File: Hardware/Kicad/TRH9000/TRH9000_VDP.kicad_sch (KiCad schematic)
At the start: 22 parts, among them U1 V9990, U2 KM428C256, U3 KM428C256, X1 14.318Mhz, Y1 21.47727Mhz

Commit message: Footprint for the V9990
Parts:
- C2: footprint (none) -> Capacitor_SMD:C_0805_2012Metric
- U1: footprint Ddraig:QFP-128_28x28_Pitch0.8mm -> trh9000:QFP-128_28x28_Pitch0.8mm
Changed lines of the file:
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@@
       (effects (font (size 1.27 1.27)) (justify left))
     )
-    (property "Footprint" "Ddraig:QFP-128_28x28_Pitch0.8mm" (id 2) (at 129.54 135.89 0)
+    (property "Footprint" "trh9000:QFP-128_28x28_Pitch0.8mm" (id 2) (at 129.54 135.89 0)
       (effects (font (size 1.27 1.27)) hide)
     )
@@
       (effects (font (size 1.27 1.27)) (justify left))
     )
-    (property "Footprint" "" (id 2) (at 49.2252 250.19 0)
+    (property "Footprint" "Capacitor_SMD:C_0805_2012Metric" (id 2) (at 49.2252 250.19 0)
       (effects (font (size 1.27 1.27)) hide)
     )

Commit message: Trimpots for the RGB coming from V9990
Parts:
- Y1: footprint Crystal:Crystal_HC50_Vertical -> Crystal:Crystal_HC49-U_Vertical
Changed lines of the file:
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@@
     (property "Reference" "Y1" (id 0) (at 54.61 145.5928 0))
     (property "Value" "21.47727Mhz" (id 1) (at 54.61 147.9042 0))
-    (property "Footprint" "Crystal:Crystal_HC50_Vertical" (id 2) (at 54.61 152.4 0)
+    (property "Footprint" "Crystal:Crystal_HC49-U_Vertical" (id 2) (at 54.61 152.4 0)
       (effects (font (size 1.27 1.27)) hide)
     )

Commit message: REV0 - Footprint Review
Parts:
- R1, R2, R3, R4, R5, R6: footprint LED_SMD:LED_0805_2012Metric -> Resistor_SMD:R_0805_2012Metric
- U2, U3: footprint (none) -> trh9000:TSOP-II-40_10.16x18.41mm_P0.8mm
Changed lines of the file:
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@@
       (effects (font (size 1.27 1.27)) (justify left))
     )
-    (property "Footprint" "" (id 2) (at 292.1 207.01 0)
+    (property "Footprint" "trh9000:TSOP-II-40_10.16x18.41mm_P0.8mm" (id 2) (at 292.1 207.01 0)
       (effects (font (size 1.27 1.27)) hide)
     )
@@
       (effects (font (size 1.27 1.27)) (justify left))
     )
-    (property "Footprint" "LED_SMD:LED_0805_2012Metric" (id 2) (at 51.562 83.82 90)
+    (property "Footprint" "Resistor_SMD:R_0805_2012Metric" (id 2) (at 51.562 83.82 90)
       (effects (font (size 1.27 1.27)) hide)
     )
@@
       (effects (font (size 1.27 1.27)) (justify left))
     )
-    (property "Footprint" "" (id 2) (at 292.1 100.33 0)
+    (property "Footprint" "trh9000:TSOP-II-40_10.16x18.41mm_P0.8mm" (id 2) (at 292.1 100.33 0)
       (effects (font (size 1.27 1.27)) hide)
     )
@@
       (effects (font (size 1.27 1.27)) (justify left))
     )
-    (property "Footprint" "LED_SMD:LED_0805_2012Metric" (id 2) (at 82.042 146.05 90)
+    (property "Footprint" "Resistor_SMD:R_0805_2012Metric" (id 2) (at 82.042 146.05 90)
       (effects (font (size 1.27 1.27)) hide)
     )
@@
       (effects (font (size 1.27 1.27)) (justify left))
     )
-    (property "Footprint" "LED_SMD:LED_0805_2012Metric" (id 2) (at 59.182 83.82 90)
+    (property "Footprint" "Resistor_SMD:R_0805_2012Metric" (id 2) (at 59.182 83.82 90)
       (effects (font (size 1.27 1.27)) hide)
     )
@@
       (effects (font (size 1.27 1.27)) (justify left))
     )
-    (property "Footprint" "LED_SMD:LED_0805_2012Metric" (id 2) (at 43.942 83.82 90)
+    (property "Footprint" "Resistor_SMD:R_0805_2012Metric" (id 2) (at 43.942 83.82 90)
       (effects (font (size 1.27 1.27)) hide)
     )
@@
     (property "Reference" "R3" (id 0) (at 54.61 135.7122 90))
     (property "Value" "10M" (id 1) (at 54.61 138.0236 90))
-    (property "Footprint" "LED_SMD:LED_0805_2012Metric" (id 2) (at 54.61 139.192 90)
+    (property "Footprint" "Resistor_SMD:R_0805_2012Metric" (id 2) (at 54.61 139.192 90)
       (effects (font (size 1.27 1.27)) hide)
     )
@@
       (effects (font (size 1.27 1.27)) (justify left))
     )
-    (property "Footprint" "LED_SMD:LED_0805_2012Metric" (id 2) (at 74.422 146.05 90)
-      (effects (font (size 1.27 1.27)) hide)
-    )
+    (property "Footprint" "Resistor_SMD:R_0805_2012Metric" (id 2) (at 74.422 146.05 90)
+      (effects (font (size 1.27 1.27)) hide)
+    )

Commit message: Routing 1. First 3d view of the current PCB.
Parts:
- U2, U3: footprint trh9000:TSOP-II-40_10.16x18.41mm_P0.8mm -> trh9000:SOJ-40_400mil
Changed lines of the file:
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@@
       (effects (font (size 1.27 1.27)) (justify left))
     )
-    (property "Footprint" "trh9000:TSOP-II-40_10.16x18.41mm_P0.8mm" (id 2) (at 292.1 207.01 0)
+    (property "Footprint" "trh9000:SOJ-40_400mil" (id 2) (at 292.1 207.01 0)
       (effects (font (size 1.27 1.27)) hide)
     )
@@
       (effects (font (size 1.27 1.27)) (justify left))
     )
-    (property "Footprint" "trh9000:TSOP-II-40_10.16x18.41mm_P0.8mm" (id 2) (at 292.1 100.33 0)
+    (property "Footprint" "trh9000:SOJ-40_400mil" (id 2) (at 292.1 100.33 0)
       (effects (font (size 1.27 1.27)) hide)
     )

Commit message: Many changes, among them, replacing the Composite out with SCART-rgb.
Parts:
- removed C2, C5, C6, C7, C8, C9: 100nF, Capacitor_SMD:C_0805_2012Metric, symbol Device:C
- removed C3: 47uF, Capacitor_THT:CP_Radial_D5.0mm_P2.50mm, symbol Device:C_Polarized
- removed L1, L2: 4.7uH, Inductor_SMD:L_1206_3216Metric, symbol pspice:INDUCTOR
- added unit 3 of U1
- added unit 2 of U1
- U1: footprint trh9000:QFP-128_28x28_Pitch0.8mm -> trh9000:LQFP-128_28x28mm_P0.8mm; MPN (none) -> V9990; Manufacturer (none) -> Yamaha
- U2, U3: Manufacturer (none) -> Samsung Electronics Inc.; Status (none) -> OBSOLETE
- X1: value 14.318Mhz -> Crystek_CE3291; footprint Oscillator:Oscillator_DIP-8 -> Oscillator:Oscillator_SMD_Abracon_ASV-4Pin_7.0x5.1mm; symbol Oscillator:CXO_DIP8 -> TRH9000:Crystek_CE3291; Frequency (none) -> 14.31818MHz; MPN (none) -> CE3291-14.318180; Manufacturer (none) -> Crystek Corporation
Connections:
- net +5V: now also R6.2, X1.4 (Vcc); no longer R6.1, U1.123 (VCC), U1.27 (VCC), U1.53 (VCC), U1.81 (VCC), U1.97 (VCC), U2.1 (VCC), U2.20 (VCC), U3.1 (VCC), U3.20 (VCC), X1.8 (Vcc)
- net B: now also U1.95 (B/D1/CB1); no longer U1.95 (B/D31/CB1)
- net G: now also U1.94 (G/D2/CB2); no longer U1.94 (G/D2/CB2)
- net GND: now also X1.2 (GND); no longer U1.1 (GND), U1.100 (GND), U1.107 (GND), U1.118 (GND), U1.17 (GND), U1.32 (GND), U1.44 (GND), U1.64 (GND), U1.75 (GND), U1.86 (GND), U2.12 (VSS), U2.21 (VSS), U2.30 (VSS), U2.40 (VSS), U3.12 (VSS), U3.21 (VSS), U3.30 (VSS), U3.40 (VSS), X1.4 (GND)
- net R: now also U1.93 (R/D3/CB3); no longer U1.93 (R/D3/CB3)
- net V0A0: now also U1.26 (V0_A0/KA0); no longer U1.26 (V0A0/KA0)
- net V0A1: now also U1.25 (V0_A1/KA1); no longer U1.25 (V0A1/KA1)
- net V0A2: now also U1.24 (V0_A2/KA2); no longer U1.24 (V0A2/KA2)
- net V0A3: now also U1.23 (V0_A3/KA3); no longer U1.23 (V0A3/KA3)
- net V0A4: now also U1.22 (V0_A4/KA4); no longer U1.22 (V0A4/KA4)
- net V0A5: now also U1.21 (V0_A5/KA5); no longer U1.21 (V0A5/KA5)
- net V0A6: now also U1.20 (V0_A6/KA6); no longer U1.20 (V0A6/KA6)
- net V0A7: now also U1.19 (V0_A7/KA7); no longer U1.19 (V0A7/KA7)
- net V0A8: now also U1.18 (V0_A8/KA8); no longer U1.18 (V0A8/KA8)
- net V0D0: now also U1.36 (V0_D0/KD0); no longer U1.36 (V0D0/DK0)
- net V0D1: now also U1.35 (V0_D1/KD1); no longer U1.35 (V0D1/DK1)
- net V0D2: now also U1.34 (V0_D2/KD2); no longer U1.34 (V0D2/DK2)
- net V0D3: now also U1.33 (V0_D3/KD3); no longer U1.33 (V0D3/DK3)
- net V0D4: now also U1.31 (V0_D4/KD4); no longer U1.31 (V0D4/DK4)
- net V0D5: now also U1.30 (V0_D5/KD5); no longer U1.30 (V0D5/DK5)
- net V0D6: now also U1.29 (V0_D6/KD6); no longer U1.29 (V0D6/DK6)
- net V0D7: now also U1.28 (V0_D7/KD7); no longer U1.28 (V0D7/DK7)
- net V0S0: now also U1.52 (V0_S0); no longer U1.52 (V0S0)
- net V0S1: now also U1.51 (V0_S1); no longer U1.51 (V0S1)
- net V0S2: now also U1.50 (V0_S2); no longer U1.50 (V0S2)
- net V0S3: now also U1.49 (V0_S3); no longer U1.49 (V0S3)
- net V0S4: now also U1.48 (V0_S4); no longer U1.48 (V0S4)
- net V0S5: now also U1.47 (V0_S5); no longer U1.47 (V0S5)
- net V0S6: now also U1.46 (V0_S6); no longer U1.46 (V0S6)
- net V0S7: now also U1.45 (V0_S7); no longer U1.45 (V0S7)
- net V1A0: now also U1.80 (V1_A0); no longer U1.80 (V1A0)
- net V1A1: now also U1.79 (V1_A1); no longer U1.79 (V1A1)
- net V1A2: now also U1.78 (V1_A2); no longer U1.78 (V1A2)
- net V1A3: now also U1.77 (V1_A3); no longer U1.77 (V1A3)
- net V1A4: now also U1.76 (V1_A4); no longer U1.76 (V1A4)
- net V1A5: now also U1.74 (V1_A5); no longer U1.74 (V1A5)
- net V1A6: now also U1.73 (V1_A6); no longer U1.73 (V1A6)
- net V1A7: now also U1.72 (V1_A7); no longer U1.72 (V1A7)
- net V1A8: now also U1.71 (V1_A8); no longer U1.71 (V1A8)
- net V1D0: now also U1.82 (V1_D0); no longer U1.82 (V1D0)
- net V1D1: now also U1.83 (V1_D1); no longer U1.83 (V1D1)
- net V1D2: now also U1.84 (V1_D2); no longer U1.84 (V1D2)
- net V1D3: now also U1.85 (V1_D3); no longer U1.85 (V1D3)
- net V1D4: now also U1.87 (V1_D4); no longer U1.87 (V1D4)
- net V1D5: now also U1.88 (V1_D5); no longer U1.88 (V1D5)
- net V1D6: now also U1.89 (V1_D6); no longer U1.89 (V1D6)
- net V1D7: now also U1.90 (V1_D7); no longer U1.90 (V1D7)
- net V1S0: now also U1.61 (V1_S0); no longer U1.61 (V1S0)
- net V1S1: now also U1.60 (V1_S1); no longer U1.60 (V1S1)
- net V1S2: now also U1.59 (V1_S2); no longer U1.59 (V1S2)
- net V1S3: now also U1.58 (V1_S3); no longer U1.58 (V1S3)
- net V1S4: now also U1.57 (V1_S4); no longer U1.57 (V1S4)
- net V1S5: now also U1.56 (V1_S5); no longer U1.56 (V1S5)
- net V1S6: now also U1.55 (V1_S6); no longer U1.55 (V1S6)
- net V1S7: now also U1.54 (V1_S7); no longer U1.54 (V1S7)
- net ~{CSYNC}: now also U1.102 (~{CSYNC/FLM}); no longer U1.102 (~{CSYNC}/FLM)
- net ~{VDPR}: now also U1.2 (~{CSW}); no longer U1.3 (~{CSR})
- net ~{VDPW}: now also U1.3 (~{CSR}); no longer U1.2 (~{CSW})
- net X2: now reaches C4.1, R3.1, Y1.2
- net X2: now also U1.99 (XTAL2); no longer U1.99 (XTAL2)
- net ~{V0_WE}: now reaches U3.13 (R~{WB}/~{WE})
- net ~{V0_WE}: now also U1.40 (~{V0_WE}); no longer U1.40 (~{V0WE})
- net ~{V0_RAS}: now reaches U3.14 (~{RAS})
- net ~{V0_RAS}: now also U1.38 (~{V0_RAS}); no longer U1.38 (~{V0RAS})
- net ~{V0_SC}: now reaches U3.2 (SC)
- net ~{V0_SC}: now also U1.42 (~{V0_SC}); no longer U1.42 (V0SC)
- net ~{V0_CAS}: now reaches U3.27 (~{CAS})
- net ~{V0_CAS}: now also U1.39 (~{V0_CAS}); no longer U1.39 (~{V0CAS})
- net ~{VO_SOE}: now reaches U3.35 (~{SE})
- net ~{VO_SOE}: now also U1.43 (~{V0_SOE}); no longer U1.43 (~{V0SOE})
- net ~{V0_TR}: now reaches U3.7 (~{DT}/~{OE})
- net ~{V0_TR}: now also U1.41 (~{V0_TR/OE}); no longer U1.41 (~{V0TR}/~{OE})
- net X1: now reaches C1.1, R3.2, Y1.1
- net X1: now also U1.98 (XTAL1); no longer U1.98 (XTAL1)
- net ~{V1_WE}: now reaches U2.13 (R~{WB}/~{WE})
- net ~{V1_WE}: now also U1.65 (~{V1_WE}); no longer U1.65 (~{V1WE})
- net ~{V1_RAS}: now reaches U2.14 (~{RAS})
- net ~{V1_RAS}: now also U1.62 (~{V1_RAS}); no longer U1.62 (~{V1RAS})
- net ~{V1_SC}: now reaches U2.2 (SC)
- net ~{V1_SC}: now also U1.67 (V1_SC); no longer U1.67 (V1SC)
- net ~{V1_CAS}: now reaches U2.27 (~{CAS})
- net ~{V1_CAS}: now also U1.63 (~{V1_CAS}); no longer U1.63 (~{V1CAS})
- net ~{V1_SOE}: now reaches U2.35 (~{SE})
- net ~{V1_SOE}: now also U1.68 (~{V1_SOE}); no longer U1.68 (~{V1SOE})
- net ~{V1_TR}: now reaches U2.7 (~{DT}/~{OE})
- net ~{V1_TR}: now also U1.66 (~{V1_TR/OE}); no longer U1.66 (~{V1TR}/~{OE})
- net HRESET: now reaches R5.2
- net HRESET: now also U1.105 (~{HRESET}/CB4); no longer U1.106 (~{VRESET}/CB5)
- net VMREQ: now reaches R4.2, U1.124 (~{VMREQ})
- removed net +5VA: U1.96 (AVCC)
- removed net GNDA: U1.92 (AGND)
- new net MCKIN: U1.113 (MCKIN), X1.3 (OUT)
- new net VRESET: R6.1, U1.106 (~{VRESET}/CB5)
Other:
- note added: "VGA clocks: ------------- 640x400 (70Hz) - 25.175 MHz 640x480 (60Hz) - 25.175 MHz Pal clocks: ------------- 704x576 (50Hz) - 4.43361875 MHz NTSC clocks: -------------- 704x480 (60Hz) - 3.579545 MHz"
- note added: "VRAM"
- note added: "Video Display Processor"
- moved on the sheet: C1, C4, R1, R2, R3, R4, R5, R6, X1, Y1

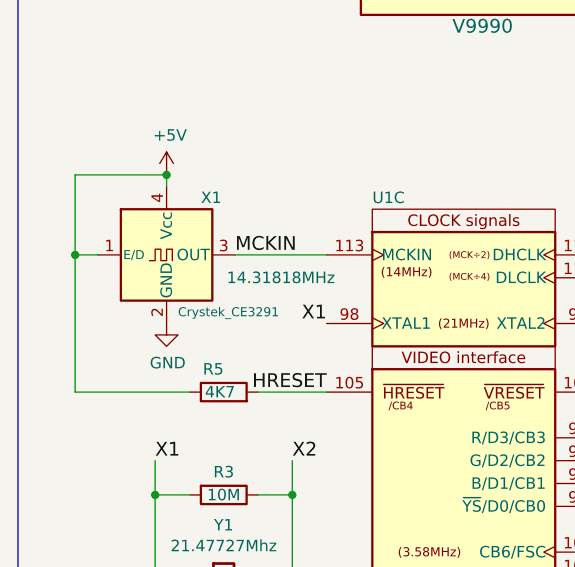
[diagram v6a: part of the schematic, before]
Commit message: Multiple updates. Routing. Almost finished routing for the VDP. Moved back the footprint for the 14mhz oscillator to THT as it is easier to find outside US/Europe and I have a bunch laying around here. Organized all components into the PCB. Removed the holed in the cartridge so I can better measure them in the standard MSX cartridge. Changed the RGB connector footprint to a shorter version so we can fit it in the standard size cartridge. Fixed multiple footprints to 0805 as we will be standardizing in that size.
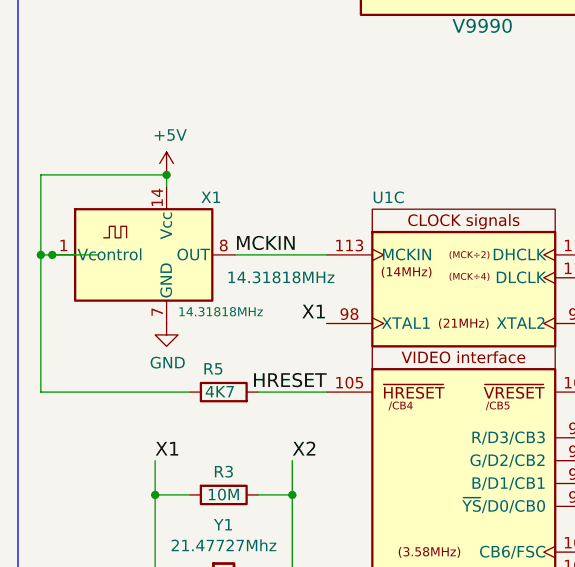
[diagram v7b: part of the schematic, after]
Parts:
- X1: value Crystek_CE3291 -> 14.31818MHz; footprint Oscillator:Oscillator_SMD_Abracon_ASV-4Pin_7.0x5.1mm -> Oscillator:Oscillator_DIP-14; symbol TRH9000:Crystek_CE3291 -> Oscillator:OCXO-14
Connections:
- net +5V: now also X1.14 (Vcc); no longer X1.4 (Vcc)
- net GND: now also X1.7 (GND); no longer X1.2 (GND)
- net MCKIN: now also X1.8 (OUT); no longer X1.3 (OUT)
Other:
- moved on the sheet: X1
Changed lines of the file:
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@@
   (junction (at 182.88 172.72) (diameter 0) (color 0 0 0 0)
   )
+  (junction (at 19.05 173.99) (diameter 0) (color 0 0 0 0)
+  )
   (junction (at 30.48 200.66) (diameter 0) (color 0 0 0 0)
   )
@@
   (junction (at 31.75 165.1) (diameter 0) (color 0 0 0 0)
   )
-  (junction (at 21.59 173.99) (diameter 0) (color 0 0 0 0)
+  (junction (at 17.78 173.99) (diameter 0) (color 0 0 0 0)
   )
   (junction (at 38.1 222.25) (diameter 0) (color 0 0 0 0)
@@
     (stroke (width 0) (type default) (color 0 0 0 0))
   )
+  (wire (pts (xy 17.78 173.99) (xy 17.78 189.23))
+    (stroke (width 0) (type default) (color 0 0 0 0))
+  )
   (bus (pts (xy 124.46 218.44) (xy 124.46 220.98))
     (stroke (width 0) (type default) (color 0 0 0 0))
@@
     (stroke (width 0) (type default) (color 0 0 0 0))
   )
+  (wire (pts (xy 19.05 173.99) (xy 24.13 173.99))
+    (stroke (width 0) (type default) (color 0 0 0 0))
+  )
   (wire (pts (xy 99.06 86.36) (xy 83.82 86.36))
     (stroke (width 0) (type default) (color 0 0 0 0))
@@
     (stroke (width 0) (type default) (color 0 0 0 0))
   )
-  (wire (pts (xy 21.59 165.1) (xy 31.75 165.1))
+  (wire (pts (xy 17.78 165.1) (xy 31.75 165.1))
     (stroke (width 0) (type default) (color 0 0 0 0))
   )
@@
     (stroke (width 0) (type default) (color 0 0 0 0))
   )
+  (wire (pts (xy 17.78 173.99) (xy 19.05 173.99))
+    (stroke (width 0) (type default) (color 0 0 0 0))
+  )
   (wire (pts (xy 128.27 198.12) (xy 147.32 198.12))
     (stroke (width 0) (type default) (color 0 0 0 0))
@@
     (stroke (width 0) (type default) (color 0 0 0 0))
   )
-  (wire (pts (xy 21.59 173.99) (xy 21.59 189.23))
+  (wire (pts (xy 17.78 165.1) (xy 17.78 173.99))
     (stroke (width 0) (type default) (color 0 0 0 0))
   )
@@
     (stroke (width 0) (type default) (color 0 0 0 0))
   )
-  (wire (pts (xy 21.59 189.23) (xy 34.29 189.23))
-    (stroke (width 0) (type default) (color 0 0 0 0))
-  )
-  (wire (pts (xy 21.59 173.99) (xy 21.59 165.1))
+  (wire (pts (xy 17.78 189.23) (xy 34.29 189.23))
     (stroke (width 0) (type default) (color 0 0 0 0))
   )
@@
   )
   (bus (pts (xy 237.49 69.85) (xy 237.49 72.39))
-    (stroke (width 0) (type default) (color 0 0 0 0))
-  )
-  (wire (pts (xy 21.59 173.99) (xy 24.13 173.99))
     (stroke (width 0) (type default) (color 0 0 0 0))
   )
@@
     (pin "1")
   )
-  (symbol (lib_id "TRH9000:Crystek_CE3291") (at 31.75 173.99 0) (unit 1)
+  (symbol (lib_id "Oscillator:OCXO-14") (at 31.75 173.99 0) (unit 1)
     (in_bom yes) (on_board yes)
     (property "Reference" "X1" (id 0) (at 35.56 167.64 0)
       (effects (font (size 1.27 1.27)) (justify left))
     )
-    (property "Value" "Crystek_CE3291" (id 1) (at 33.02 180.34 0)
+    (property "Value" "14.31818MHz " (id 1) (at 33.02 180.34 0)
       (effects (font (size 1 1)) (justify left))
     )
-    (property "Footprint" "Oscillator:Oscillator_SMD_Abracon_ASV-4Pin_7.0x5.1mm" (id 2) (at 43.18 182.88 0)
+    (property "Footprint" "Oscillator:Oscillator_DIP-14" (id 2) (at 43.18 182.88 0)
       (effects (font (size 1.27 1.27)) hide)
     )
-    (property "Datasheet" "https://www.crystek.com/crystal/spec-sheets/clock/C32xx-C39xx.pdf" (id 3) (at 34.29 186.69 0)
+    (property "Datasheet" "http://www.petermann-technik.de/fileadmin/petermann/pdf/crystal-oscillators/OCXO-14_PETERMANN-TECHNIK.pdf" (id 3) (at 24.13 171.45 0)
       (effects (font (size 1.27 1.27)) hide)
     )
-    (property "Manufacturer" "Crystek Corporation" (id 4) (at 52.07 163.83 0)
+    (property "Frequency" "14.31818MHz " (id 6) (at 44.45 176.53 0))
+    (property "Manufacturer" "Crystek Corporation" (id 5) (at 52.07 163.83 0)
       (effects (font (size 1.27 1.27)) hide)
     )
-    (property "MPN" "CE3291-14.318180" (id 5) (at 52.07 166.37 0)
+    (property "MPN" "CE3291-14.318180" (id 6) (at 52.07 166.37 0)
       (effects (font (size 1.27 1.27)) hide)
     )
-    (property "Frequency" "14.31818MHz " (id 6) (at 44.45 176.53 0))
     (pin "1")
-    (pin "2")
-    (pin "3")
-    (pin "4")
+    (pin "14")
+    (pin "7")
+    (pin "8")
   )
   (symbol (lib_id "Device:C") (at 30.48 215.9 0) (unit 1)

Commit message: Routing, readme, etc
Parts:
- X1: footprint Oscillator:Oscillator_DIP-14 -> Oscillator:Oscillator_DIP-8; symbol Oscillator:OCXO-14 -> Oscillator:CXO_DIP8
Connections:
- net +5V: now also X1.8 (Vcc); no longer X1.14 (Vcc)
- net GND: now also X1.4 (GND); no longer X1.7 (GND)
- net MCKIN: now also X1.5 (OUT); no longer X1.8 (OUT)
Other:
- moved on the sheet: X1
